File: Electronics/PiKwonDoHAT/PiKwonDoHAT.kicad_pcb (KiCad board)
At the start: 2 copper layers, 60.2 x 63 mm, 42 parts, among them CN1 Conn_02x20_Odd_Even, CN2 Judge1, CN3 Judge2, CN4 Judge3, CN5 Controller, U1 74LV1T34, U2 74LV1T34, U3 74LV1T34, U4 74LV1T34

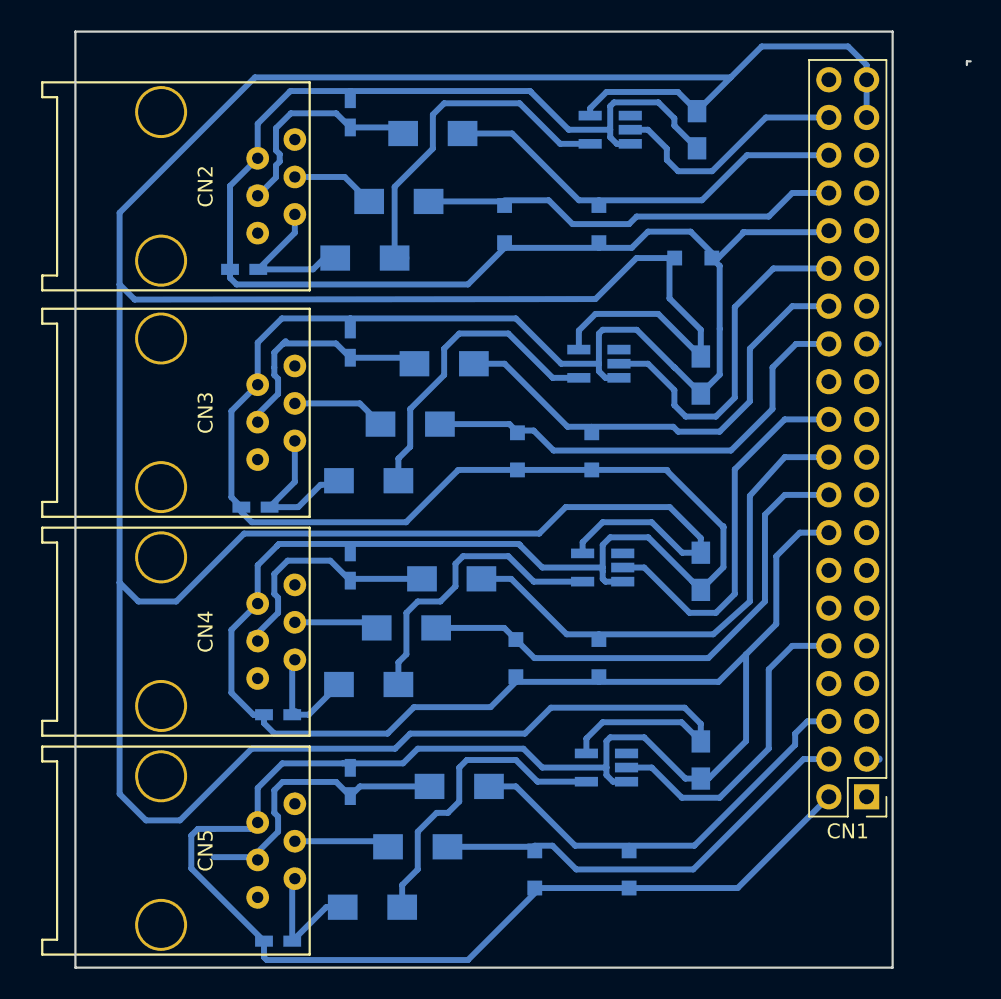
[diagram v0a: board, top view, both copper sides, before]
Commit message: Initial HAT manufacturing file preparation
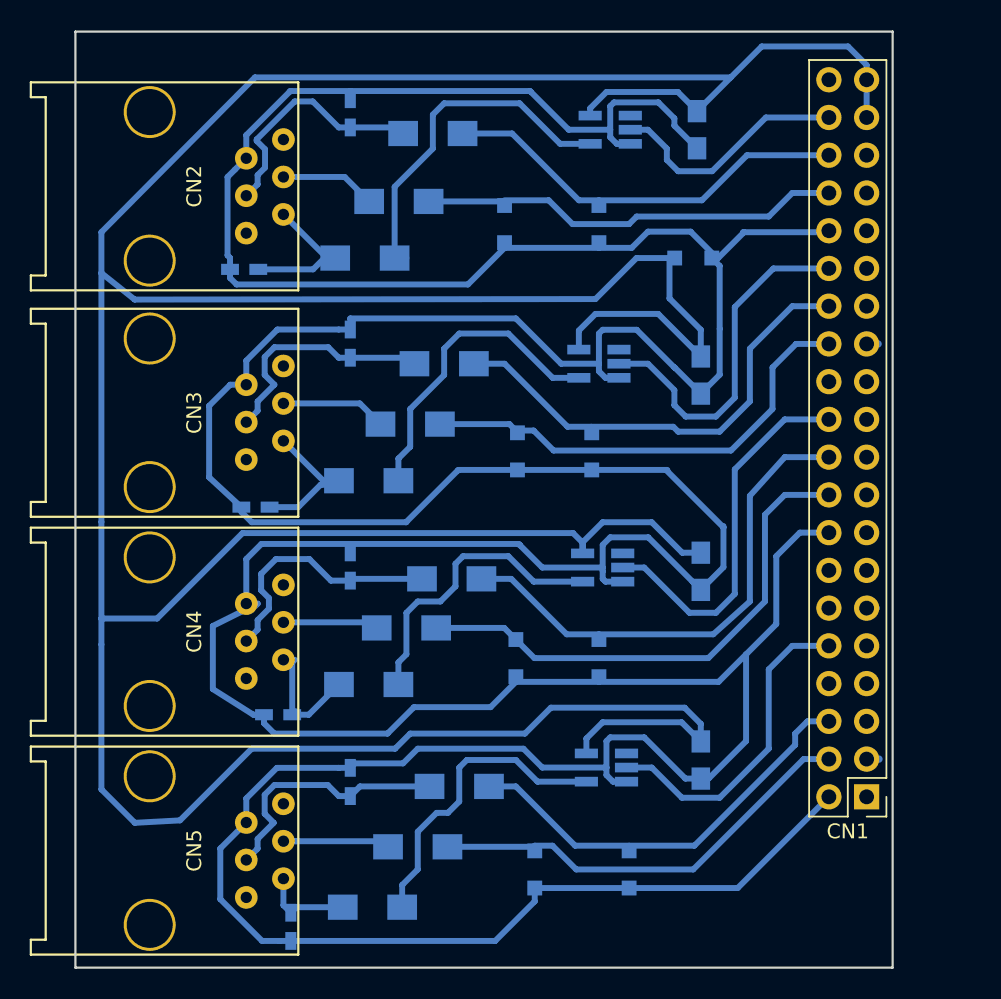
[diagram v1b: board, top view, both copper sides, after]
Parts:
- moved C12 1.29 mm to (84.5, 130.2), turned to 270 degrees
- moved CN2 0.77 mm to (75.0, 80.4)
- moved CN3 0.77 mm to (75.0, 95.7)
- moved CN4 0.77 mm to (75.0, 110.4)
- moved CN5 0.77 mm to (75.0, 125.1)
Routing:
- net +5V: track 276.2 -> 270.8 mm
- net Net-(C11-Pad1): track 19.7 -> 17.3 mm
- net Net-(C12-Pad1): track 8.38 -> 6.15 mm
- net Net-(CN5-Pad4): track 6.53 -> 7.53 mm
- net GND: track 402.9 -> 402.0 mm
- net Net-(C9-Pad1): track 16.7 -> 17.3 mm
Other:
- board size 60.2 x 63 mm -> 55 x 63 mm

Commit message: Updated HAT PCB slightly
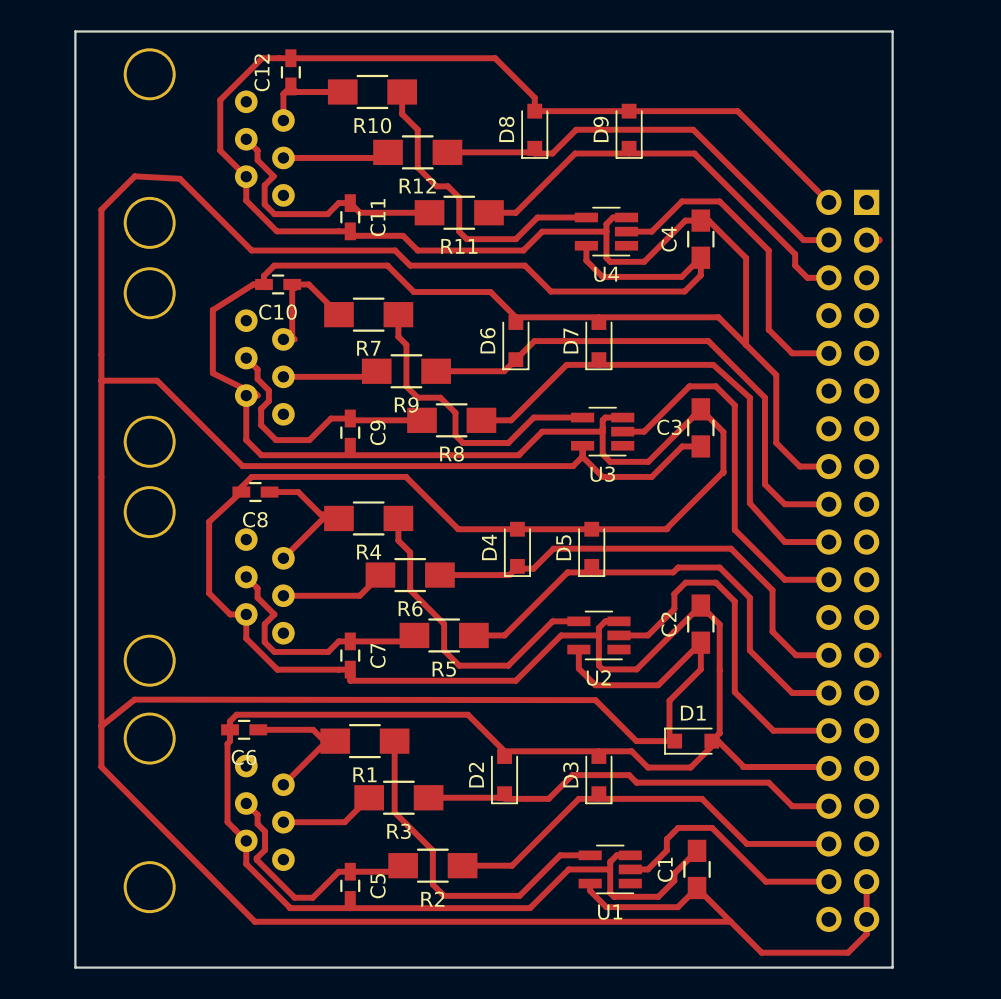
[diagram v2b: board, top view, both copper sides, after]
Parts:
- C1, C10, C11, C12, C2, C3, C4, C5, C6, C7, C8, C9, D1, D2, D3, D4, D5, D6, D7, D8, D9, R1, R10, R11, R12, R2, R3, R4, R5, R6, R7, R8, R9, U1, U2, U3, U4: moved to F.Cu
- CN1, CN2, CN3, CN4, CN5: moved to B.Cu
- moved C12 57.5 mm to (84.5, 72.7), turned to 90 degrees
- moved R10 54.9 mm to (90.0, 74.1)
- moved C5 52.0 mm to (88.5, 127.5), turned to 270 degrees
- moved C1 49.8 mm to (111.8, 126.4), turned to 90 degrees
- moved D8 49.8 mm to (100.9, 76.6), turned to 90 degrees
- moved D9 49.8 mm to (107.3, 76.6), turned to 90 degrees
- moved U1 49.8 mm to (106.0, 126.4)
- moved R2 49.3 mm to (94.1, 126.1)
- moved CN5 47.2 mm to (75.0, 77.9), turned to 270 degrees
- moved R12 46.7 mm to (93.0, 78.1)
- moved CN2 42.2 mm to (75.0, 122.6), turned to 270 degrees
- moved R3 40.1 mm to (91.8, 121.6)
- moved CN1 40.0 mm to (123.2, 81.5)
- moved R11 38.6 mm to (95.8, 82.2)
- moved C11 38.0 mm to (88.5, 82.5), turned to 270 degrees
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
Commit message: Trace widening for manufacturing and assembly ese
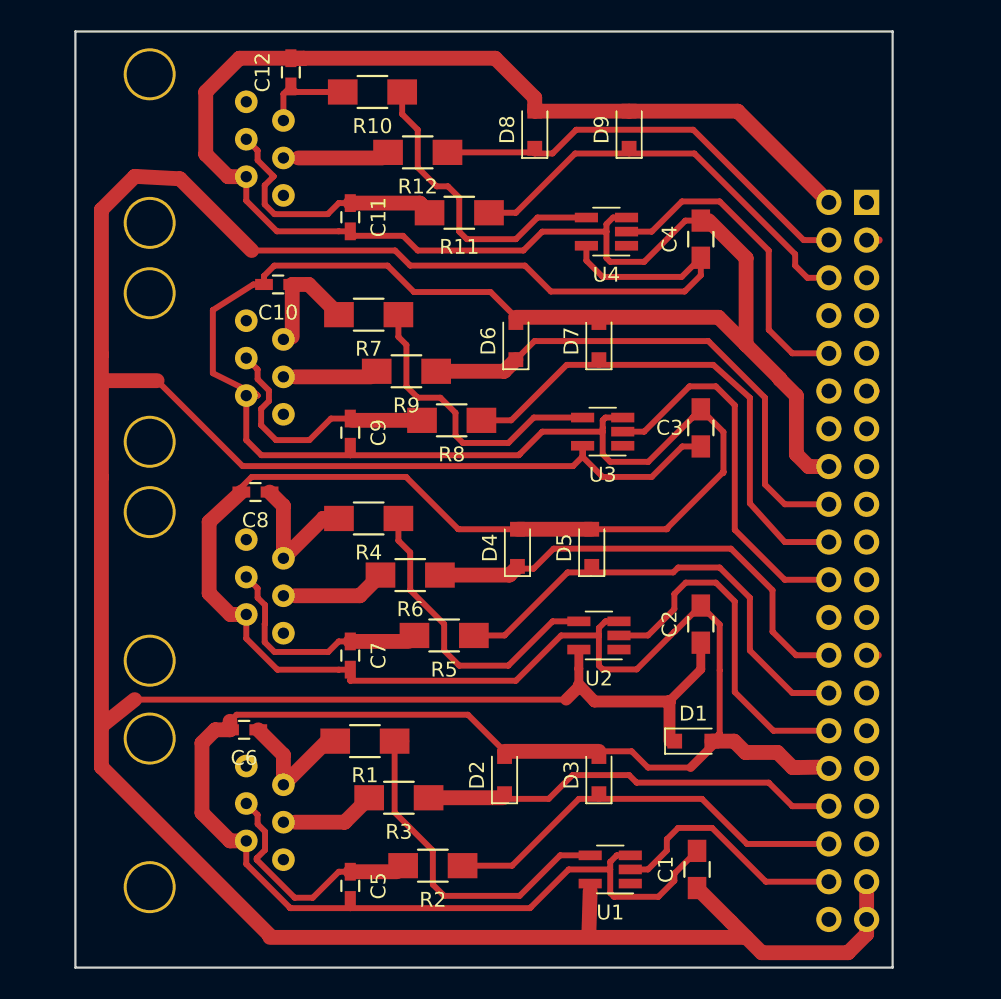
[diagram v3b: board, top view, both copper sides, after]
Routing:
- net +5V: track 270.8 -> 258.1 mm
- net GND: track 402.0 -> 407.9 mm
- net Net-(C8-Pad1): track 10.7 -> 11.5 mm
- net Net-(C7-Pad1): track 16.3 -> 15.7 mm

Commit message: Updated HAT trace widths
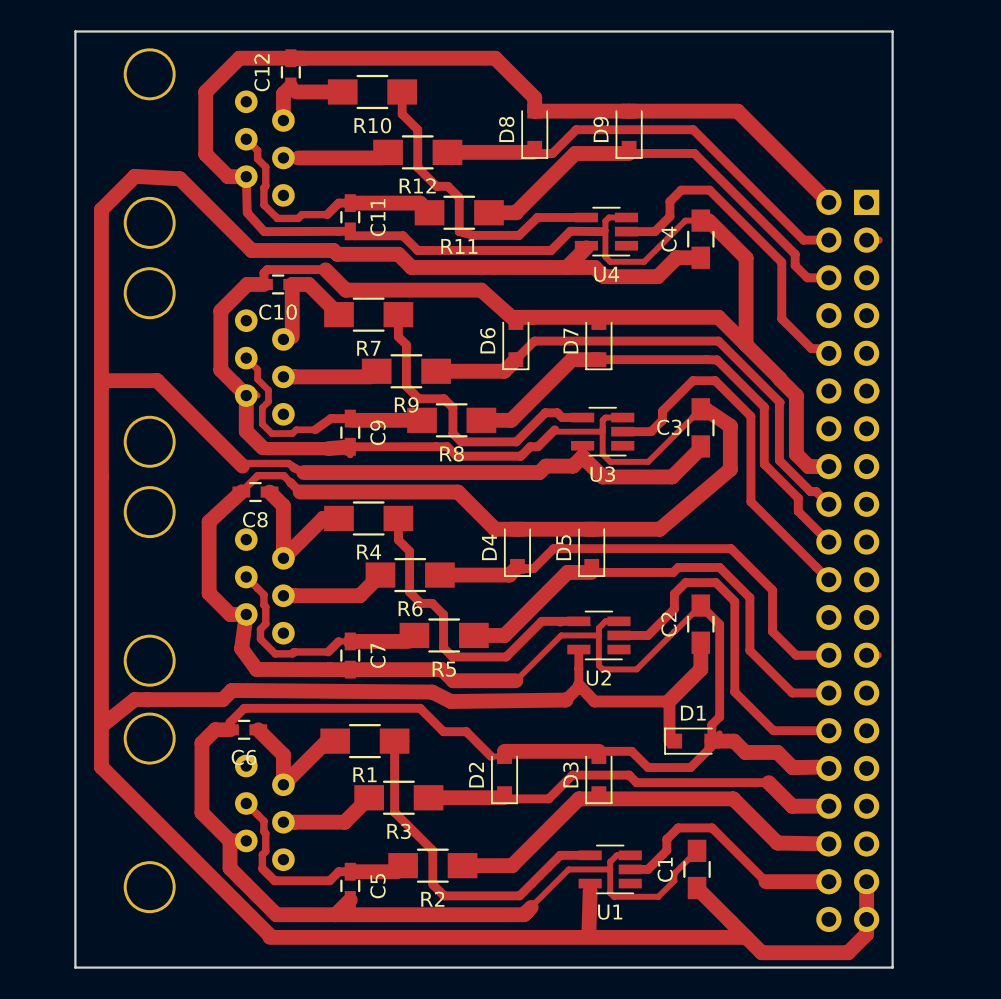
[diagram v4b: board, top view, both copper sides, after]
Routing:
- net +5V: track 258.1 -> 250.5 mm
- net GND: track 407.9 -> 410.4 mm
- net /J3_LOAD: track 34.0 -> 32.9 mm
- net Net-(C5-Pad1): track 16.4 -> 15.3 mm
- net /J3_DATA: track 35.2 -> 34.2 mm
- net /J3_CLK: track 25.4 -> 24.6 mm
- net Net-(CN4-Pad4): track 5.67 -> 6.43 mm
- net Net-(CN3-Pad4): track 6.34 -> 7.11 mm
- net Net-(CN2-Pad4): track 6.02 -> 6.78 mm
- net Net-(C9-Pad1): track 17.3 -> 16.6 mm
- net Net-(C7-Pad1): track 15.7 -> 16.3 mm
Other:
- rule trace_min: 0.2 -> 0.4

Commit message: Updated library footprint references
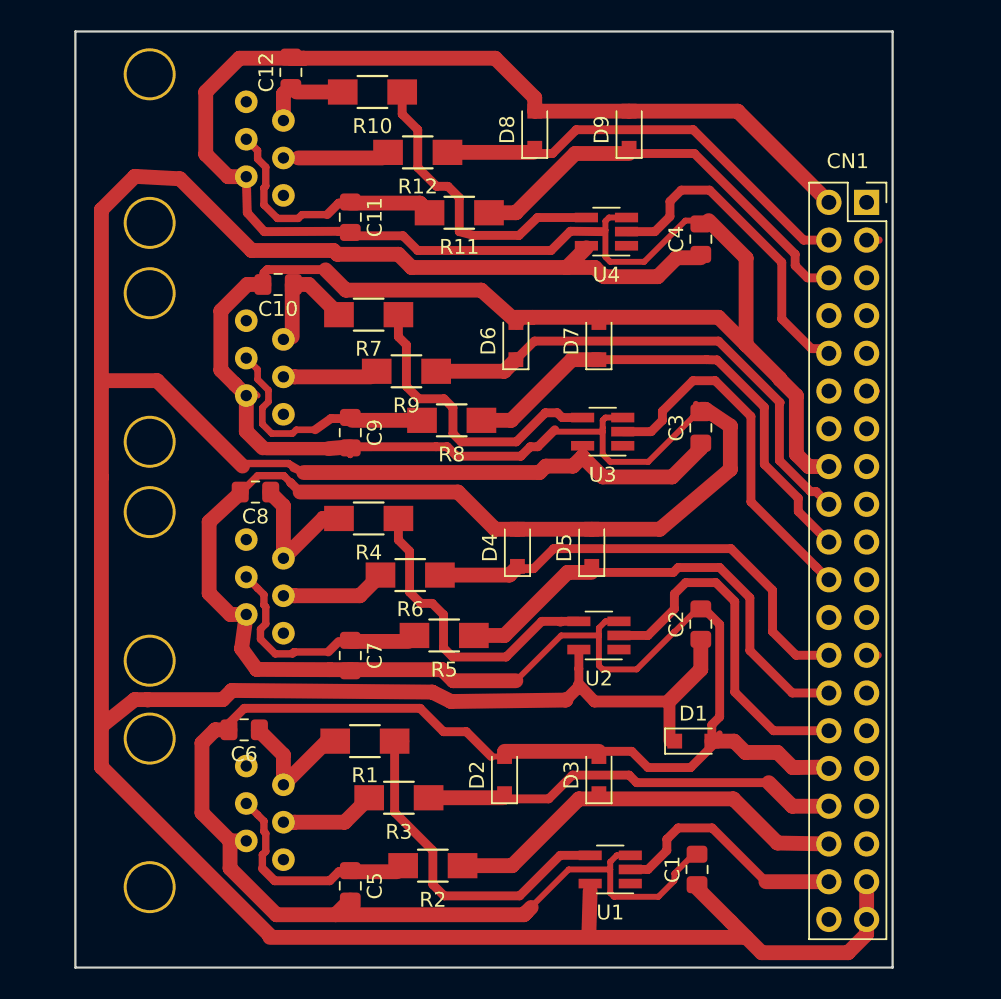
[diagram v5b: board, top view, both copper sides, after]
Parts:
- C1, C2, C3, C4: footprint Capacitors_SMD:C_0805_HandSoldering -> Capacitor_SMD:C_0805_2012Metric_Pad1.15x1.40mm_HandSolder
- C10, C11, C12, C5, C6, C7, C8, C9: footprint Capacitors_SMD:C_0603_HandSoldering -> Capacitor_SMD:C_0805_2012Metric_Pad1.15x1.40mm_HandSolder
- CN1: footprint Pin_Headers:Pin_Header_Straight_2x20_Pitch2.54mm -> Connector_PinSocket_2.54mm:PinSocket_2x20_P2.54mm_Vertical; moved to F.Cu
- turned CN1 to 0 degrees

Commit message: Updated zener diode footprint and layout
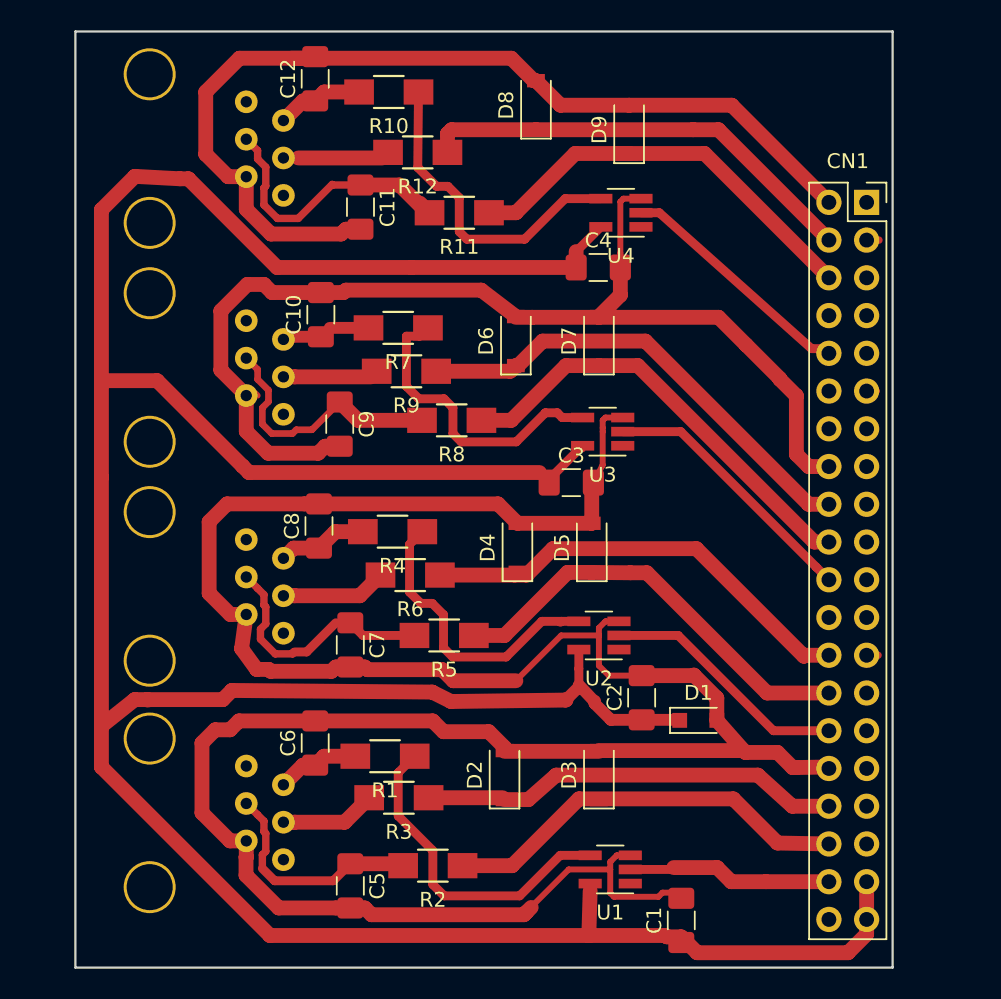
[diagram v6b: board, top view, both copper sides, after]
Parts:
- C1, C10, C11, C12, C2, C3, C4, C5, C6, C7, C8, C9: footprint Capacitor_SMD:C_0805_2012Metric_Pad1.15x1.40mm_HandSolder -> Capacitor_SMD:C_1206_3216Metric_Pad1.42x1.75mm_HandSolder
- D2, D3, D4, D5, D6, D7, D8, D9: footprint Diodes_SMD:D_SOD-323_HandSoldering -> Diode_SMD:D_SOD-123
- moved C3 9.46 mm to (103.4, 100.4), turned to 0 degrees
- moved C4 7.16 mm to (105.2, 85.9), turned to 0 degrees
- moved C2 6.35 mm to (108.1, 114.8)
- moved C6 4.86 mm to (86.1, 117.9), turned to 90 degrees
- moved C8 4.85 mm to (86.4, 103.3), turned to 90 degrees
- moved C1 3.59 mm to (110.8, 129.8)
- moved C10 3.52 mm to (86.5, 89.0), turned to 90 degrees
- moved R7 2.18 mm to (91.7, 89.9)
- moved R4 1.84 mm to (91.3, 103.7)
- moved C12 1.69 mm to (86.1, 73.2)
- moved R1 1.69 mm to (90.8, 118.8)
- moved D8 1.65 mm to (101.0, 75.0)
- moved U4 1.60 mm to (106.7, 82.2)
- moved D1 1.44 mm to (111.9, 116.4)
- moved R10 1.10 mm to (91.1, 74.1)
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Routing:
- net GND: track 410.4 -> 322.2 mm
- net +5V: track 250.5 -> 220.4 mm
- net /J2_CLK: track 23.9 -> 16.8 mm
- net /J3_CLK: track 24.6 -> 18.0 mm
- net /C_CLK: track 22.2 -> 16.3 mm
- net Net-(C8-Pad1): track 11.5 -> 6.09 mm
- net Net-(C6-Pad1): track 10.0 -> 5.63 mm
- net /J3_LOAD: track 32.9 -> 29.8 mm
- net /J1_CLK: track 16.9 -> 14.3 mm
- net /J2_LOAD: track 31.4 -> 29.0 mm
- net /J3_DATA: track 34.2 -> 31.8 mm
- net Net-(C10-Pad1): track 8.49 -> 6.30 mm
- net Net-(C11-Pad1): track 17.2 -> 19.2 mm
- net Net-(R1-Pad1): track 23.5 -> 22.1 mm
- net Net-(R10-Pad1): track 20.5 -> 21.9 mm
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
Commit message: Updated manufacturing files
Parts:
- moved C1 3.47 mm to (111.3, 126.4)
- moved R9 2.24 mm to (94.5, 92.9)
- moved R3 2.12 mm to (93.9, 121.6)
- moved R6 1.86 mm to (94.4, 106.6)
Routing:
- net GND: track 322.2 -> 318.0 mm
- net +5V: track 220.4 -> 223.4 mm
- net Net-(R7-Pad1): track 20.4 -> 17.5 mm
- net /J1_DATA: track 29.0 -> 26.6 mm
- net Net-(CN4-Pad4): track 6.43 -> 8.68 mm
- net /J3_DATA: track 31.8 -> 29.6 mm
- net /J2_DATA: track 30.2 -> 28.3 mm
- net Net-(CN3-Pad4): track 7.11 -> 8.68 mm
- net Net-(CN2-Pad4): track 6.78 -> 8.23 mm
- net Net-(R4-Pad1): track 20.0 -> 18.8 mm
- net Net-(R1-Pad1): track 22.1 -> 21.2 mm
- added copper zone on F.Cu, net GND
